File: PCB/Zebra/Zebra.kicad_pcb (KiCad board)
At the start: 2 copper layers, 19 x 93 mm, 17 parts, among them J1 Conn_01x05, J2 Conn_01x04, SW1 SW_Push, SW2 SW_Push, SW3 SW_Push, SW4 SW_Push

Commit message: Switch to foostan's footprint library, MIT license
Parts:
- SW1, SW2, SW3, SW4: footprint keyswitches:Kailh_socket_MX_optional -> kbd:CherryMX_Hotswap
- turned SW1 to 180 degrees
- turned SW2 to 180 degrees
- turned SW3 to 180 degrees
- turned SW4 to 180 degrees
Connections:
- SW1 pad 1: Net-(D1-Pad2) -> Net-(J1-Pad1)
- SW1 pad 2: Net-(J1-Pad1) -> Net-(D1-Pad2)
- SW2 pad 1: Net-(D2-Pad2) -> Net-(J1-Pad1)
- SW2 pad 2: Net-(J1-Pad1) -> Net-(D2-Pad2)
- SW3 pad 1: Net-(D3-Pad2) -> Net-(J1-Pad1)
- SW3 pad 2: Net-(J1-Pad1) -> Net-(D3-Pad2)
- SW4 pad 1: Net-(D4-Pad2) -> Net-(J1-Pad1)
- SW4 pad 2: Net-(J1-Pad1) -> Net-(D4-Pad2)
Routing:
- net Net-(J1-Pad1): track 141.6 -> 96.4 mm
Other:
- board text added: "Zebra Stripe v02"
- board text removed: "Zebra Stripe v01"

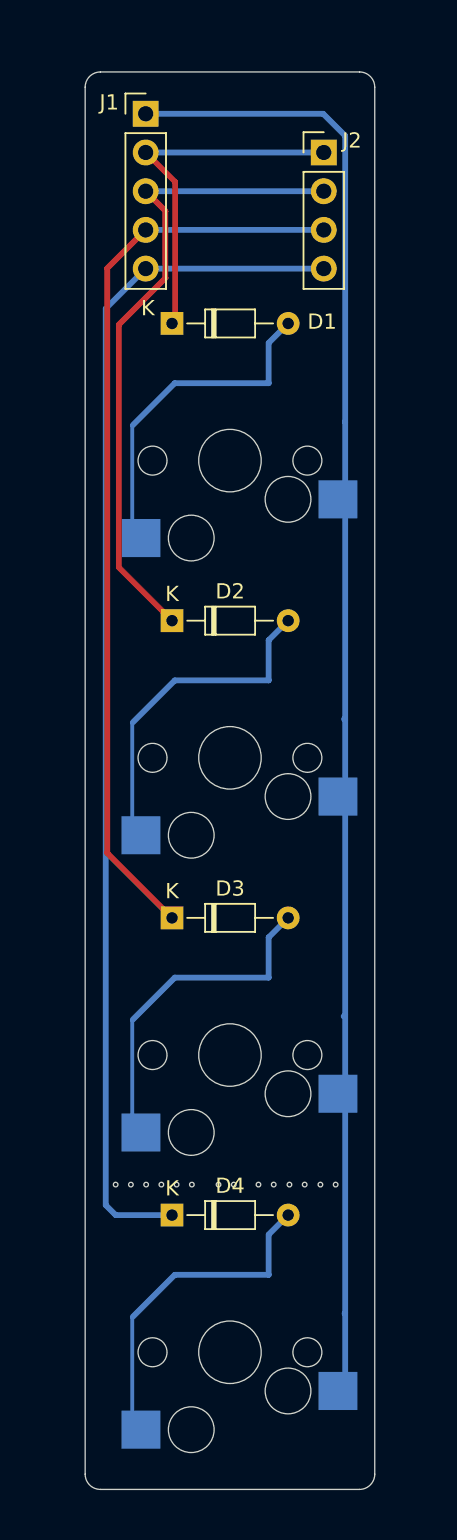
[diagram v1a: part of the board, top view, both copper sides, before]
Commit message: Add encoders
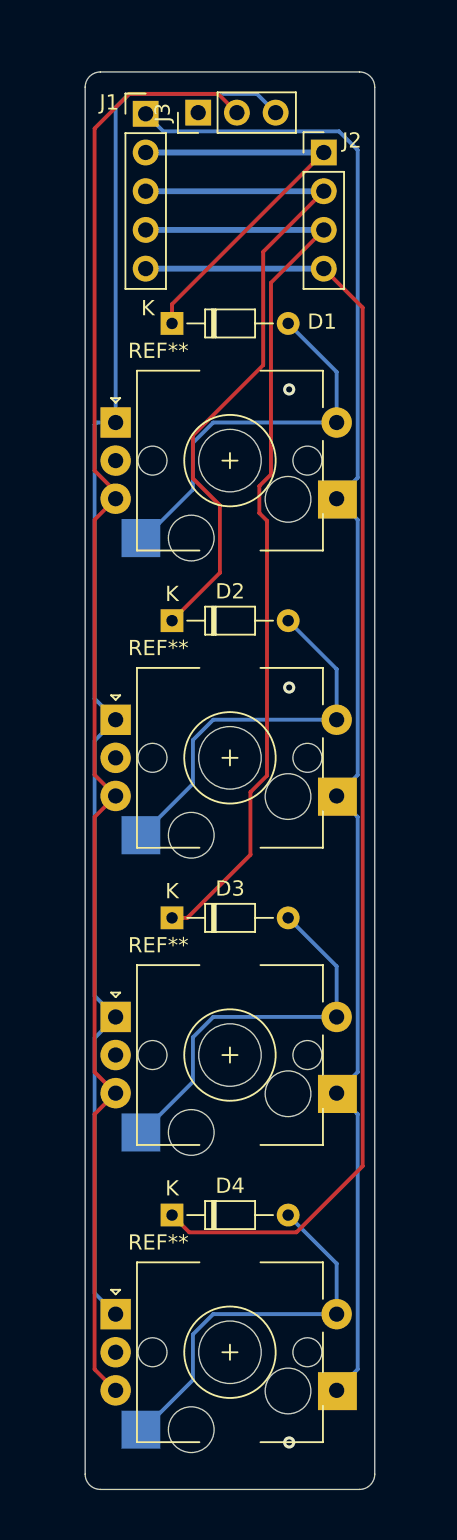
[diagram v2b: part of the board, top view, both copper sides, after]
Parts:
- removed REF** (x7): hole-03mm, holes:hole-03mm
- removed SW1, SW2, SW3, SW4: SW_Push, kbd:CherryMX_Hotswap
- added J3: Conn_01x03, Connector_PinHeader_2.54mm:PinHeader_1x03_P2.54mm_Vertical, F.Cu at (97.9, 18.7)
- added SW5: Rotary_Encoder_Switch, nk:CherryMX_Hotswap_Encoder, F.Cu at (100.0, 41.5)
- added SW6: Rotary_Encoder_Switch, nk:CherryMX_Hotswap_Encoder, F.Cu at (100.0, 61.0)
- added SW7: Rotary_Encoder_Switch, nk:CherryMX_Hotswap_Encoder, F.Cu at (100.0, 80.5)
- added SW8: Rotary_Encoder_Switch, nk:CherryMX_Hotswap_Encoder, F.Cu at (100.0, 100.0)
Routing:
- net Net-(J3-Pad2): track 0.00 -> 97.6 mm
- net Net-(J3-Pad3): track 0.00 -> 94.7 mm
- net Net-(D4-Pad1): track 78.8 -> 86.4 mm
- net Net-(J1-Pad1): track 96.4 -> 100.3 mm
- net Net-(D1-Pad2): track 22.3 -> 25.6 mm
- net Net-(D4-Pad2): track 22.3 -> 25.5 mm
- net Net-(D1-Pad1): track 23.8 -> 27.0 mm
- net Net-(D3-Pad2): track 22.3 -> 25.5 mm
- net Net-(D2-Pad2): track 22.3 -> 25.5 mm
- net Net-(D2-Pad1): track 43.1 -> 45.5 mm
- net Net-(D3-Pad1): track 59.6 -> 61.9 mm
- net GND: vias 0 -> 3
- added copper zone on B.Cu, net GND
- added copper zone on F.Cu, net GND
- removed copper zone on B.Cu, net (none)
- removed copper zone on F.Cu, net (none)

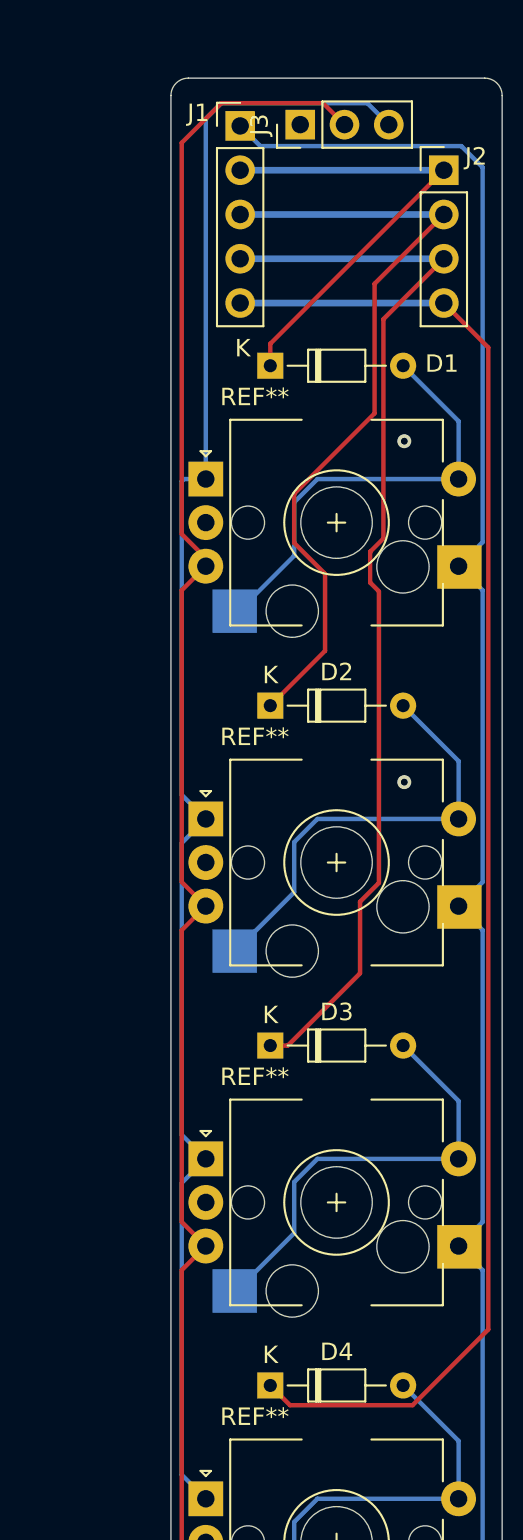
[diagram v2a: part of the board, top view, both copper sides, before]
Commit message: Rename switches, renumber
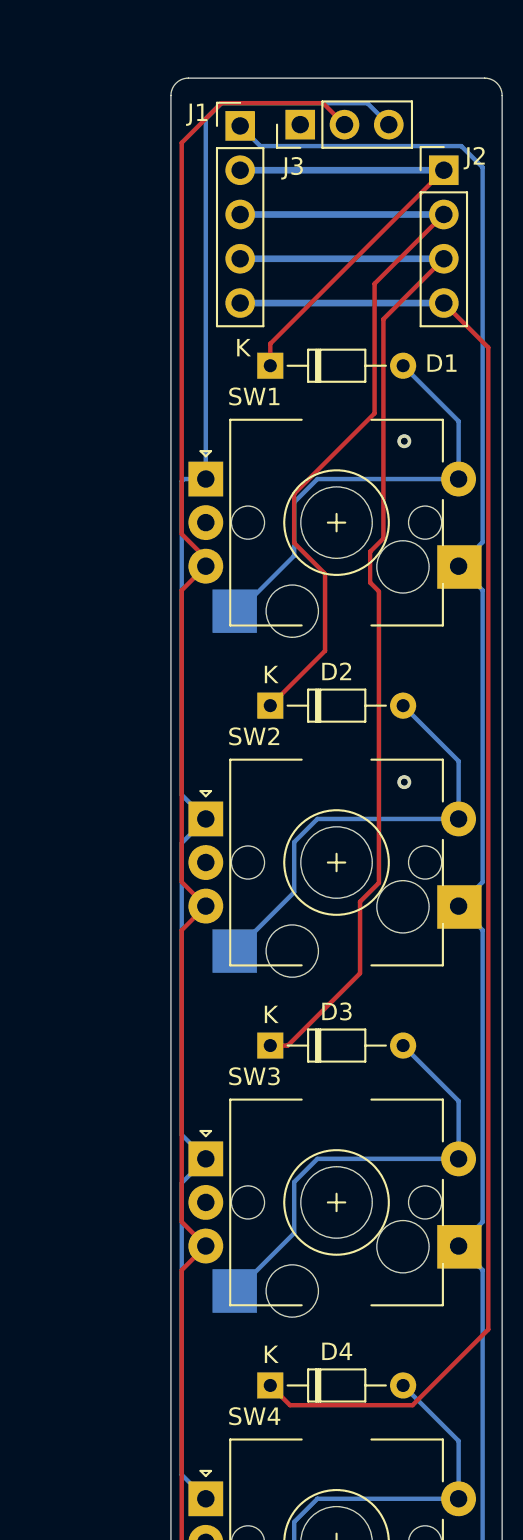
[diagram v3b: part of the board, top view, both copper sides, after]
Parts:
- renumbered SW5 to SW1, SW6 to SW2, SW7 to SW3, SW8 to SW4

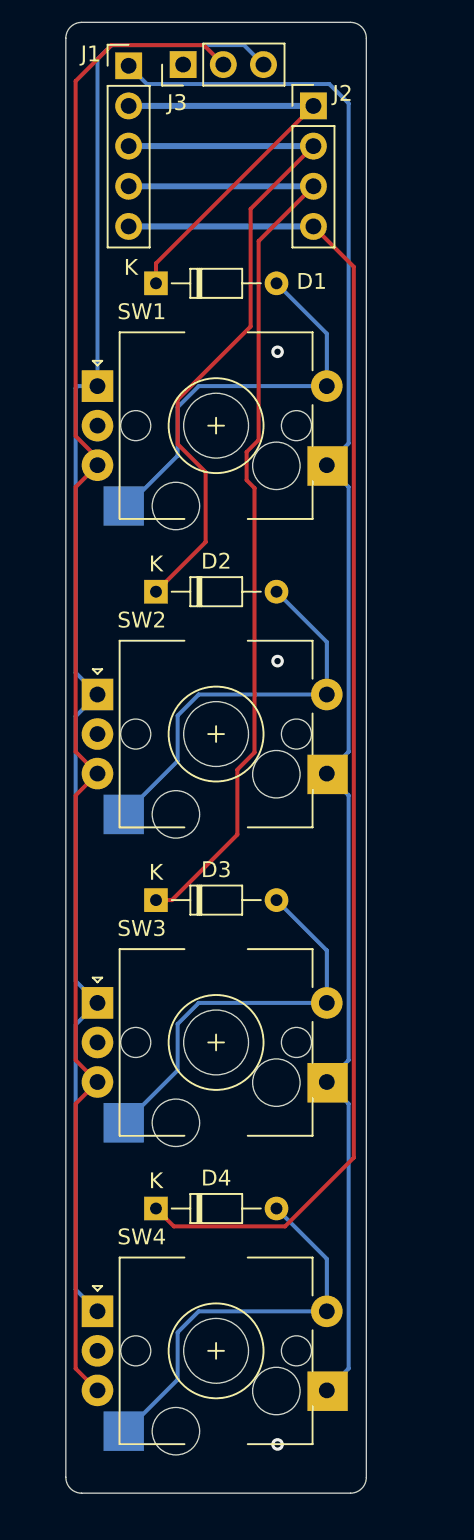
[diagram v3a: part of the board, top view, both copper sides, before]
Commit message: Add mounting holes to the stripe
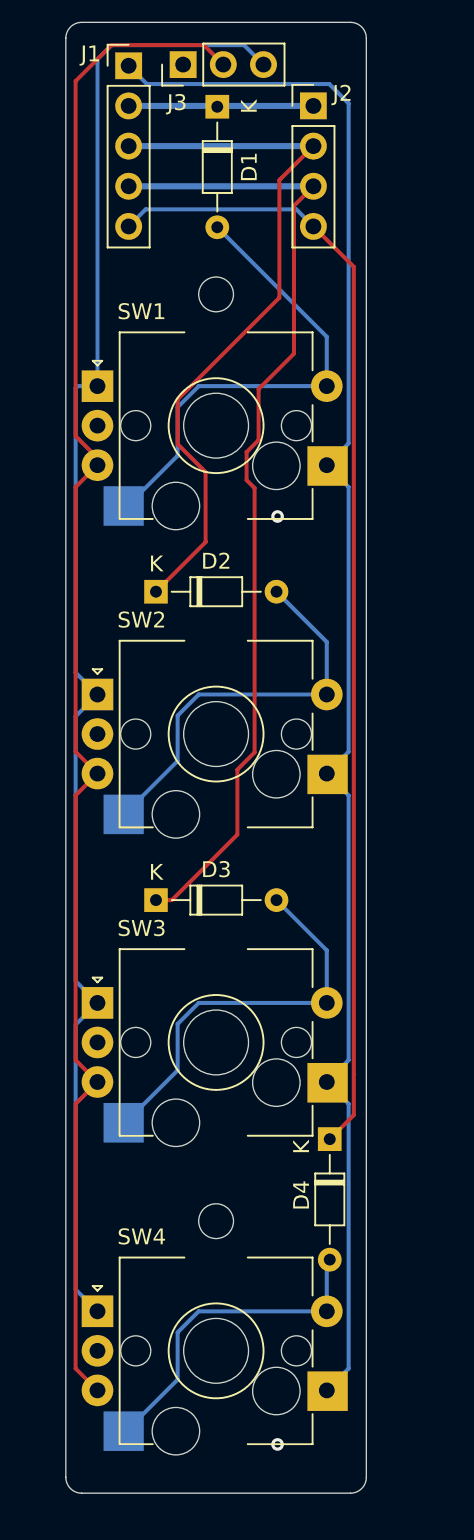
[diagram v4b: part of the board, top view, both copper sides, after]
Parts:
- added  : MountingHole_2.2mm_M2, MountingHole:MountingHole_2.2mm_M2, F.Cu at (100.0, 91.8)
- added REF**: MountingHole_2.2mm_M2, MountingHole:MountingHole_2.2mm_M2, F.Cu at (100.0, 33.2)
- moved D4 11.8 mm to (107.2, 86.6), turned to 270 degrees
- moved D1 11.8 mm to (100.1, 21.3), turned to 270 degrees
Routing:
- net Net-(D1-Pad1): track 27.0 -> 11.7 mm
- net Net-(D4-Pad1): track 86.4 -> 72.0 mm
- net Net-(D1-Pad2): track 25.6 -> 30.7 mm
- net Net-(D4-Pad2): track 25.5 -> 21.1 mm
- net GND: vias 3 -> 2
